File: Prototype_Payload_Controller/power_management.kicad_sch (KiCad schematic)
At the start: 57 parts, among them U1 INA219AxDCN, U2 LT8612, U3 LT8612, U4 LT8612

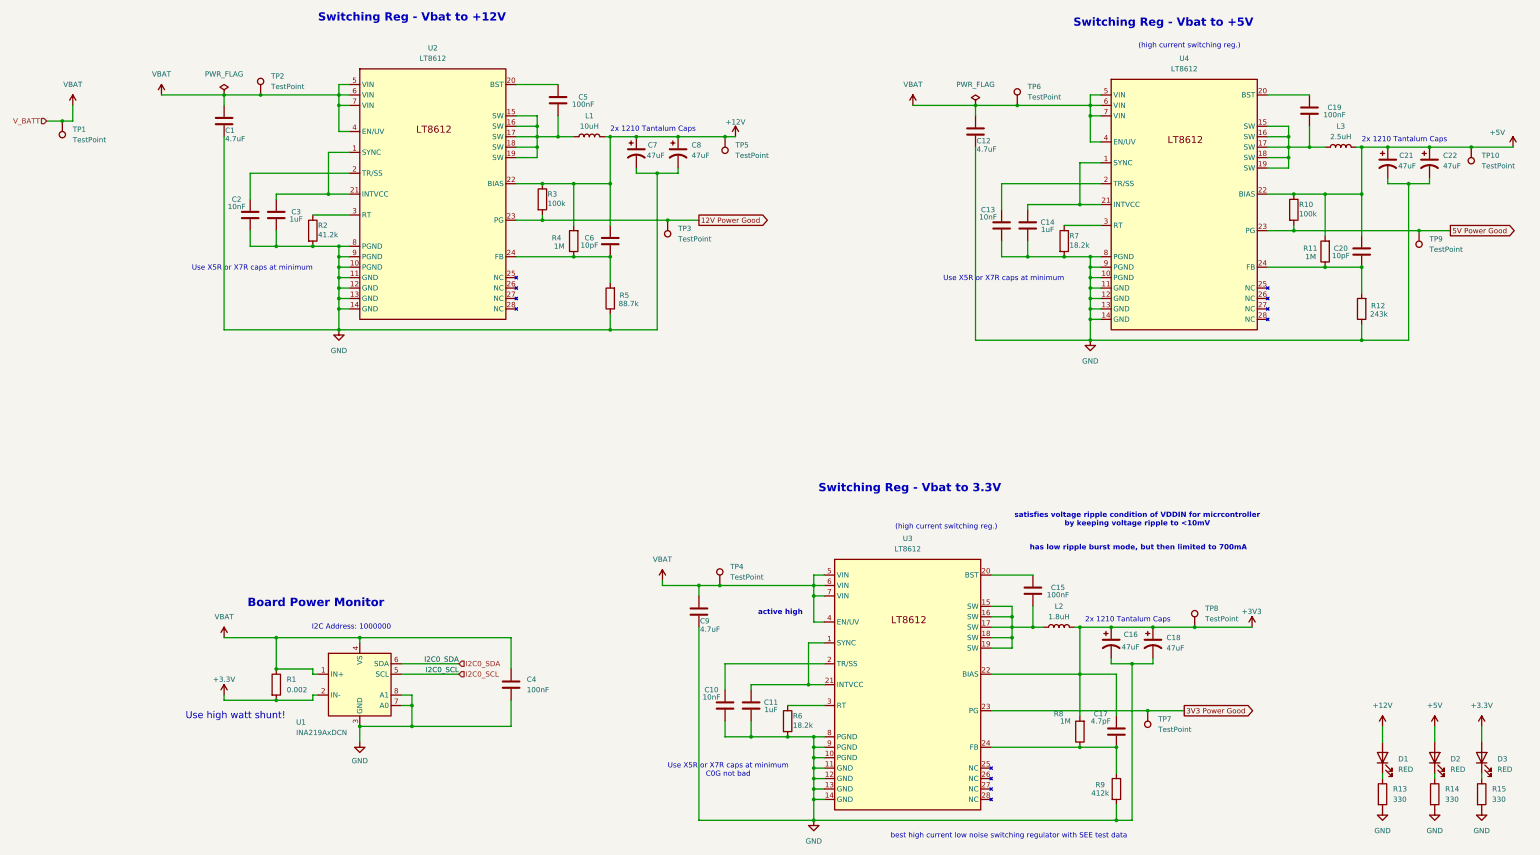
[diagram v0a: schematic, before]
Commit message: Updated Schematics to be more legible and added more datasheet pictures
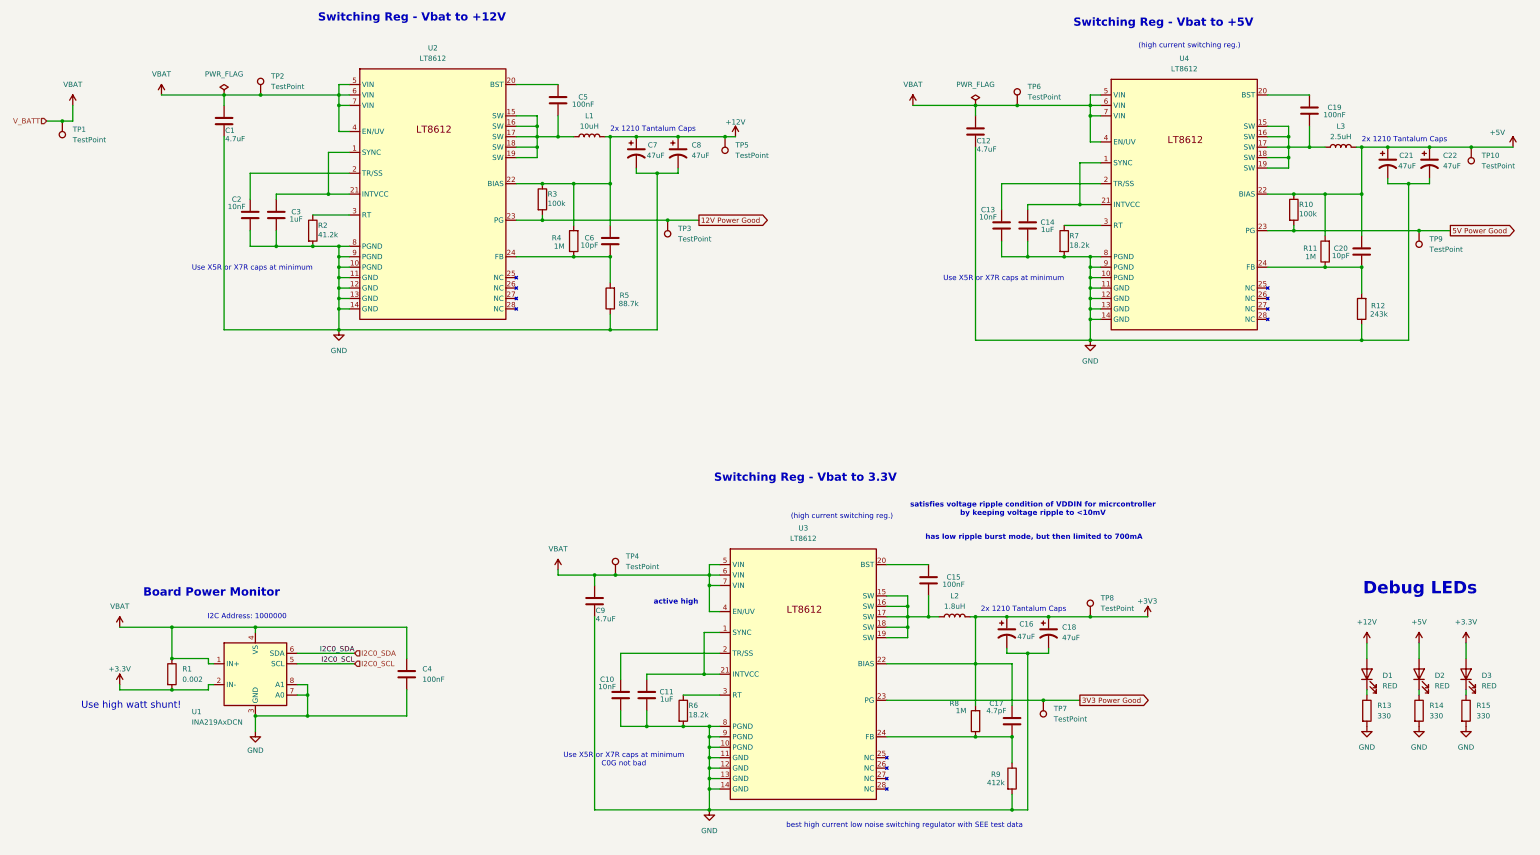
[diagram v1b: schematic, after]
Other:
- note added: "Debug LEDs"
- moved on the sheet: C10, C11, C15, C16, C17, C18, C4, C9, D1, D2, D3, L2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
